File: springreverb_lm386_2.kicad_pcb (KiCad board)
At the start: 2 copper layers, 69.9 x 55.3 mm, 49 parts, among them J1 IN, J10 FromSW, J13 FromGND, J14 From, J15 VR_3_1, J16 VR4_1, J2 Vin, J3 GND, J4 VR1_3, J5 toC6, J6 toC7, J7 VR2_3, J8 VR_2_2, J9 To, U1 TL072, U2 TC1044S, U3 LM386

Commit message: 一旦配置完了
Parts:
- removed C12: 1000u, Capacitor_THT:CP_Radial_D13.0mm_P5.00mm
- removed C13, C17, C18: 0.1u, Capacitor_THT:C_Rect_L4.0mm_W2.5mm_P2.50mm
- removed C14: 0.047u, MyLibrary:9.3_4.3_p7.5
- removed C15, C16, C19: 100u, Capacitor_THT:CP_Radial_D7.5mm_P2.50mm
- removed C20: 0.022uF, MyLibrary:9.3_4.3_p7.5
- removed J10: FromSW, MyLibrary:PinHeader_1x01_P2.54mm_Vertical
- removed R10: 2.2k, Resistor_THT:R_Axial_DIN0204_L3.6mm_D1.6mm_P7.62mm_Horizontal
- removed R11: 220k, Resistor_THT:R_Axial_DIN0204_L3.6mm_D1.6mm_P2.54mm_Vertical
- removed R8: 10, Resistor_THT:R_Axial_DIN0204_L3.6mm_D1.6mm_P7.62mm_Horizontal
- removed R9: 470, Resistor_THT:R_Axial_DIN0204_L3.6mm_D1.6mm_P7.62mm_Horizontal
- removed U3: LM386, MyLibrary:CERDIP-8_W7.62mm_SideBrazed_Socket
- added J12: FromGND, MyLibrary:PinHeader_1x01_P2.54mm_Vertical, F.Cu at (89.5, 105.0)
- added R4: 4k, Resistor_THT:R_Axial_DIN0204_L3.6mm_D1.6mm_P7.62mm_Horizontal, F.Cu at (82.0, 101.6)
- added R5: 10, Resistor_THT:R_Axial_DIN0204_L3.6mm_D1.6mm_P7.62mm_Horizontal, F.Cu at (92.5, 83.8)
- C10: value 10u -> 100u; footprint Capacitor_THT:CP_Radial_D5.0mm_P2.50mm -> Capacitor_THT:CP_Radial_D7.5mm_P2.50mm
- C11: value 100u -> 0.022uF; footprint Capacitor_THT:CP_Radial_D10.0mm_P2.50mm -> MyLibrary:9.3_4.3_p7.5
- C2: value 1000u -> 100u; footprint Capacitor_THT:CP_Radial_D13.0mm_P5.00mm -> Capacitor_THT:CP_Radial_D7.5mm_P2.50mm
- C3: value 100u -> 470p; footprint Capacitor_THT:CP_Radial_D7.5mm_P2.50mm -> MyLibrary:9.3_4.3_p7.5
- C4: footprint Capacitor_THT:C_Rect_L4.0mm_W2.5mm_P2.50mm -> Capacitor_THT:C_Disc_D5.0mm_W2.5mm_P2.50mm
- C5: value 4700p -> 0.1u; footprint MyLibrary:9.3_4.3_p7.5 -> Capacitor_THT:C_Disc_D5.0mm_W2.5mm_P5.00mm
- C6: value 470p -> 10u; footprint MyLibrary:9.3_4.3_p7.5 -> Capacitor_THT:CP_Radial_D6.3mm_P2.50mm
- C8: value 10u -> 100u; footprint Capacitor_THT:CP_Radial_D5.0mm_P2.50mm -> Capacitor_THT:CP_Radial_D10.0mm_P2.50mm
- C9: value 10u -> 0.047u; footprint Capacitor_THT:CP_Radial_D6.3mm_P2.50mm -> MyLibrary:9.3_4.3_p7.5
- J13: value FromGND -> From
- J14: value From -> VR4_1
- J15: value VR_3_1 -> VR4_3
- J16: value VR4_1 -> OUT_GND
- J2: value Vin -> IN_GND
- J3: value GND -> +15v
- J4: value VR1_3 -> -15v
- J5: value toC6 -> GND2
- J6: value toC7 -> +15v2
- R3: value 10 -> 10k
- R6: value 10 -> 2.2k
- R7: value 470 -> 220k; footprint Resistor_THT:R_Axial_DIN0204_L3.6mm_D1.6mm_P7.62mm_Horizontal -> Resistor_THT:R_Axial_DIN0204_L3.6mm_D1.6mm_P2.54mm_Vertical
- U2: value TC1044S -> LM386
- moved J4 51.4 mm to (95.8, 118.9), turned to 0 degrees
- moved C5 48.3 mm to (95.8, 115.3)
- moved U1 45.3 mm to (83.1, 120.7), turned to 90 degrees
- moved J9 38.5 mm to (97.5, 84.8), turned to 90 degrees
- moved C11 36.5 mm to (77.2, 112.5), turned to -90 degrees
- moved J5 35.3 mm to (92.3, 94.9)
- moved C1 34.7 mm to (105.3, 113.8), turned to -90 degrees
- moved R2 34.5 mm to (101.6, 117.3), turned to 90 degrees
- moved J14 33.7 mm to (72.4, 116.6), turned to 0 degrees
- moved C8 32.5 mm to (71.0, 86.1), turned to -90 degrees
- moved J15 32.4 mm to (77.1, 120.0)
- moved J16 29.9 mm to (93.0, 100.1)
- moved C3 26.9 mm to (84.8, 95.2), turned to 0 degrees
- moved U2 24.0 mm to (79.8, 90.9)
- moved C6 23.0 mm to (75.8, 97.8)
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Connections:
- C10 pad 1: GND -> Net-(C10-Pad1)
- C10 pad 2: Net-(U2-VOUT) -> Net-(J10-In)
- C11 pad 1: Net-(U3-BYPASS) -> Net-(C11-Pad1)
- C11 pad 2: GND -> Net-(J15-Pin_1)
- C2 pad 1: Net-(C2-Pad1) -> Net-(J14-Pin_1)
- C2 pad 2: GND -> Net-(C2-Pad2)
- C3 pad 1: Net-(J16-Pin_1) -> Net-(U2-+)
- C3 pad 2: Net-(J4-Pin_1) -> Net-(C3-Pad2)
- C4 pad 1: Net-(C2-Pad1) -> Net-(J3-Pin_1)
- C4 pad 2: GND -> GND1
- C5 pad 1: Net-(U3-+) -> Net-(J4-Pin_1)
- C5 pad 2: Net-(J5-Pin_1) -> GND1
- C6 pad 1: Net-(U3-+) -> Net-(C6-Pad1)
- C6 pad 2: Net-(J6-Pin_1) -> Net-(J7-Pin_1)
- C8 pad 1: Net-(U2-CAP+) -> Net-(U2-BYPASS)
- C8 pad 2: Net-(U2-CAP-) -> GND2
- C9 pad 2: Net-(J7-Pin_1) -> Net-(C10-Pad1)
- J13 pad 1: GND -> Net-(J11-In)
- J14 pad 1: Net-(J12-In) -> Net-(J14-Pin_1)
- J16 pad 1: Net-(J16-Pin_1) -> GND1
- J2 pad 1: Net-(J2-Pin_1) -> GND1
- J3 pad 1: GND -> Net-(J3-Pin_1)
- J5 pad 1: Net-(J5-Pin_1) -> GND2
- J9 pad 1: Net-(J11-In) -> Net-(J10-In)
- R2 pad 2: GND -> GND1
- R3 pad 1: Net-(C2-Pad1) -> Net-(C3-Pad2)
- R3 pad 2: Net-(J2-Pin_1) -> Net-(C2-Pad2)
- R6 pad 1: Net-(U2-VOUT) -> Net-(U1B--)
- R6 pad 2: Net-(C12-Pad2) -> GND1
- R7 pad 1: Net-(C12-Pad2) -> Net-(C11-Pad1)
- R7 pad 2: Net-(U1C-V-) -> Net-(U1B--)
- U1 pad 1: Net-(J16-Pin_1) -> Net-(J14-Pin_1)
- U1 pad 2: Net-(J16-Pin_1) -> Net-(J14-Pin_1)
- U1 pad 4: Net-(U1C-V-) -> Net-(J4-Pin_1)
- U1 pad 5: Net-(J12-In) -> Net-(J11-In)
- U1 pad 7: Net-(C20-Pad1) -> Net-(C11-Pad1)
- U1 pad 8: Net-(U1C-V+) -> Net-(J3-Pin_1)
- U2 pad 1: Net-(J2-Pin_1) -> Net-(C6-Pad1)
- U2 pad 2: Net-(U2-CAP+) -> GND2
- U2 pad 3: GND -> Net-(U2-+)
- U2 pad 4: Net-(U2-CAP-) -> GND2
- U2 pad 5: Net-(U2-VOUT) -> Net-(C10-Pad1)
- U2 pad 6: unconnected-(U2-LV-Pad6) -> Net-(J6-Pin_1)
- U2 pad 7: unconnected-(U2-OSC-Pad7) -> Net-(U2-BYPASS)
- U2 pad 8: Net-(J2-Pin_1) -> Net-(J8-Pin_1)
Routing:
- net GND: track 197.5 -> 0.00 mm, vias 2 -> 0
- net Net-(C2-Pad1): track 45.8 -> 0.00 mm
- net GND1: track 0.00 -> 35.4 mm
- net Net-(J2-Pin_1): track 34.6 -> 0.00 mm, vias 2 -> 0
- net GND2: track 0.00 -> 33.7 mm
- net Net-(J14-Pin_1): track 0.00 -> 31.5 mm
- net Net-(C12-Pad2): track 30.4 -> 0.00 mm
- net Net-(U1C-V-): track 27.0 -> 0.00 mm
- net Net-(U1B--): track 9.47 -> 32.7 mm
- net Net-(C10-Pad1): track 0.00 -> 19.1 mm
- net Net-(U3-BYPASS): track 17.8 -> 0.00 mm
- net Net-(C11-Pad1): track 0.00 -> 17.6 mm
- net Net-(J16-Pin_1): track 15.5 -> 0.00 mm
- net Net-(U1C-V+): track 15.2 -> 0.00 mm
- net Net-(U2-BYPASS): track 0.00 -> 13.2 mm
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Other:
- board size 69.9 x 55.3 mm -> 43 x 59 mm

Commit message: 配置を修正
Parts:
- moved C4 3.81 mm to (82.8, 109.2)
- moved J8 2.05 mm to (76.2, 79.8)
- moved J9 0.72 mm to (98.0, 85.3)
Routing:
- net GND1: track 35.4 -> 41.5 mm
- net Net-(J3-Pin_1): track 11.5 -> 9.71 mm
- net Net-(J10-In): track 5.48 -> 4.76 mm
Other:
- board size 43 x 59 mm -> 43.7 x 58.2 mm

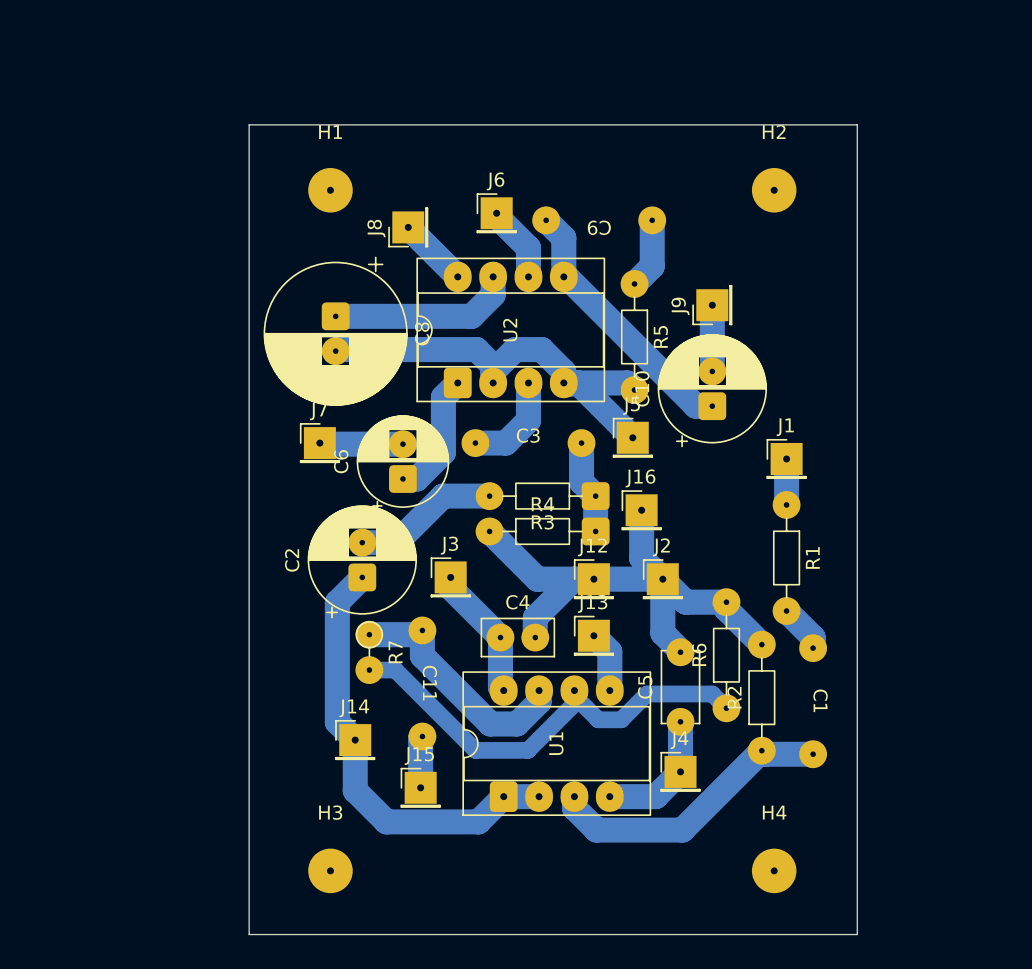
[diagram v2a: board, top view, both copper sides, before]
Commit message: GDNベタを追加
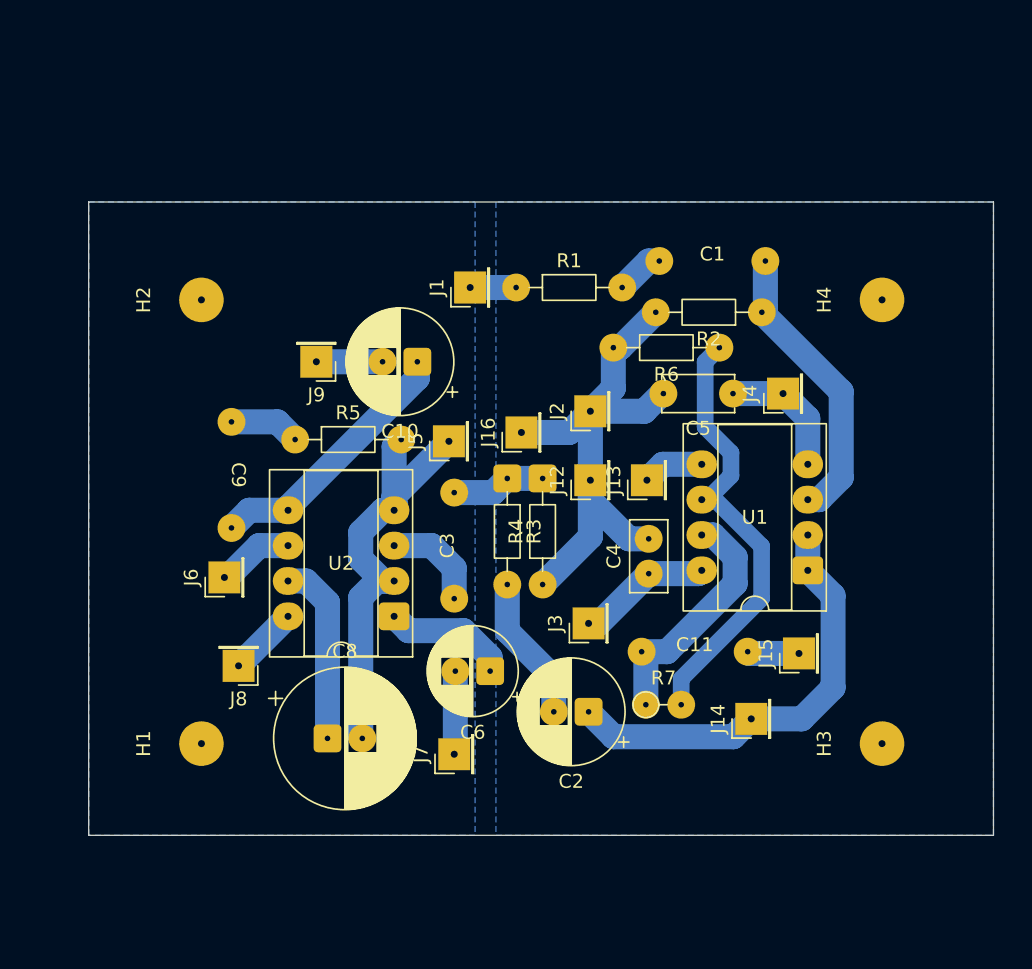
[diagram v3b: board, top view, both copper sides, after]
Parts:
- moved H2 41.9 mm to (61.3, 85.0), turned to 90 degrees
- moved H4 41.7 mm to (110.2, 85.0), turned to 90 degrees
- moved H1 40.8 mm to (61.3, 116.8), turned to 90 degrees
- moved H3 40.7 mm to (110.2, 116.8), turned to 90 degrees
- moved J8 33.8 mm to (64.0, 111.3), turned to 180 degrees
- moved J6 32.7 mm to (63.0, 104.9), turned to 90 degrees
- moved C1 32.4 mm to (98.0, 82.2), turned to 0 degrees
- moved C9 32.1 mm to (63.5, 97.5), turned to -90 degrees
- moved R2 31.5 mm to (101.6, 85.9), turned to 180 degrees
- moved C8 30.3 mm to (70.4, 116.5), turned to 0 degrees
- moved J15 28.8 mm to (104.3, 110.4), turned to 90 degrees
- moved J9 28.7 mm to (69.6, 89.4), turned to 180 degrees
- moved J14 28.5 mm to (100.8, 115.1), turned to 90 degrees
- moved J4 28.2 mm to (103.1, 91.7), turned to 90 degrees
- moved U1 27.2 mm to (104.9, 104.4), turned to 180 degrees
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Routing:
- added copper zone on B.Cu, net GND1
- added copper zone on B.Cu, net GND2
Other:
- board size 43.7 x 58.2 mm -> 65 x 45.5 mm
